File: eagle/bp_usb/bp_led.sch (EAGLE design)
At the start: 13 parts, among them J1 111-0703-001, J2 111-0702-001, J3 111-0703-001, J4 111-0702-001, J5 TSM-105-01-S-SV

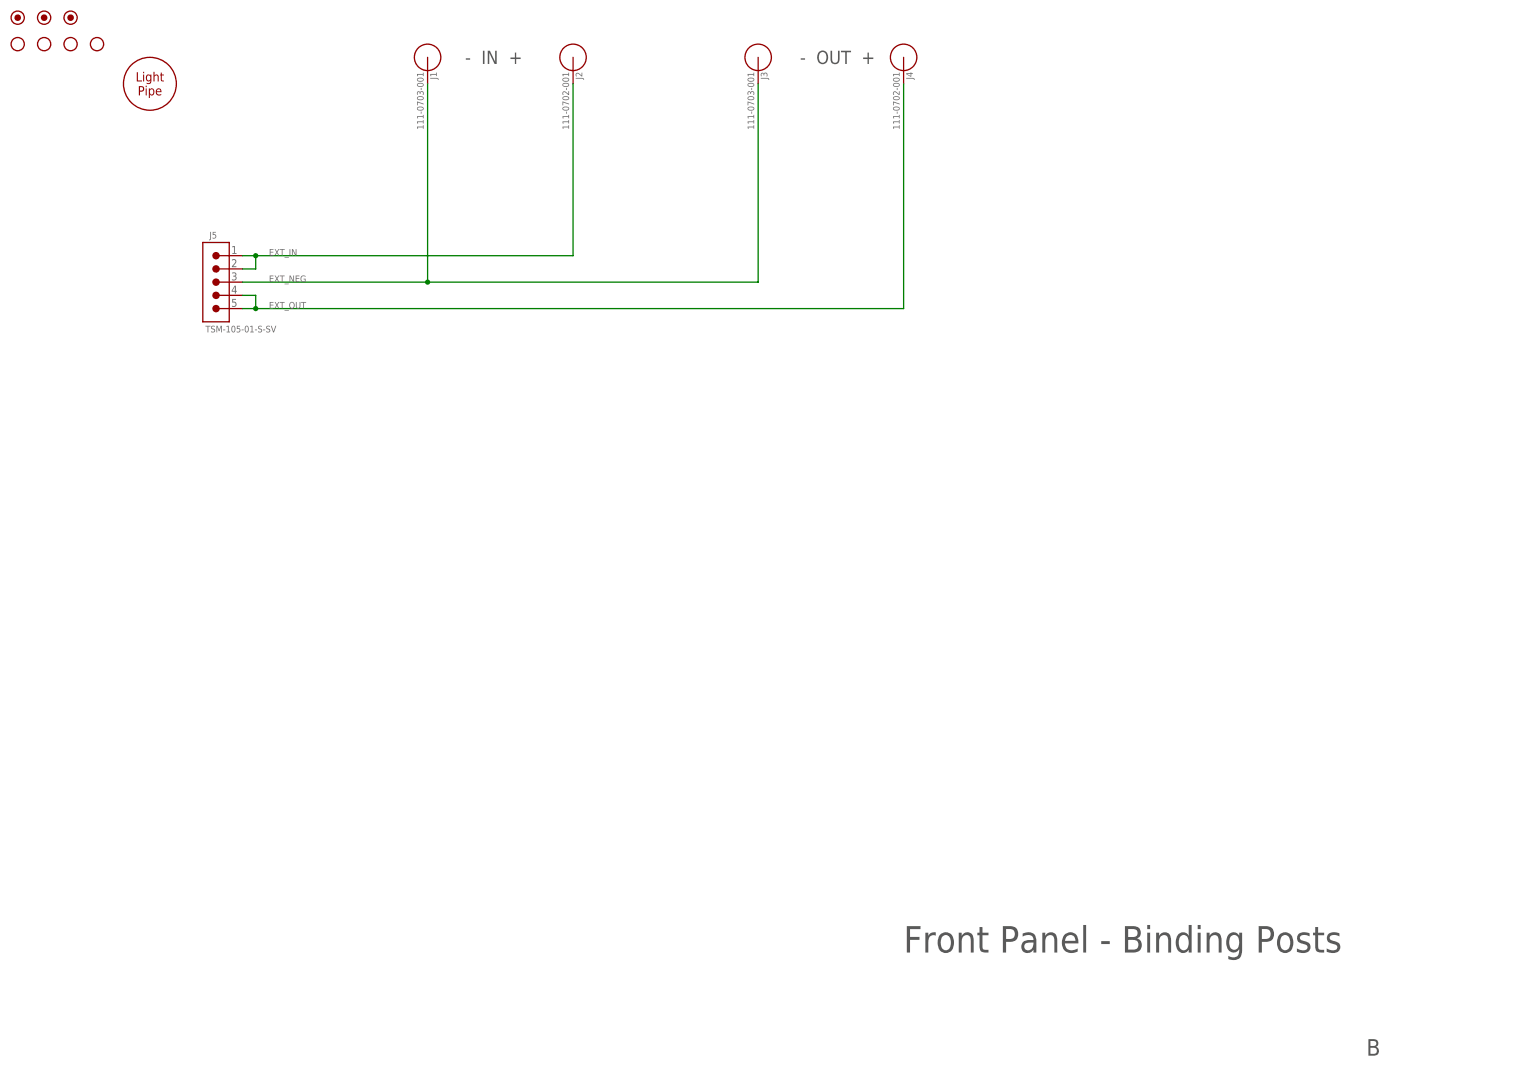
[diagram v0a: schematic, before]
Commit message: Pre-production update.
* Increased clearances from chassis/enclosure ground.
* Improved text.
* Added gerbers.
* Added USB back panel.
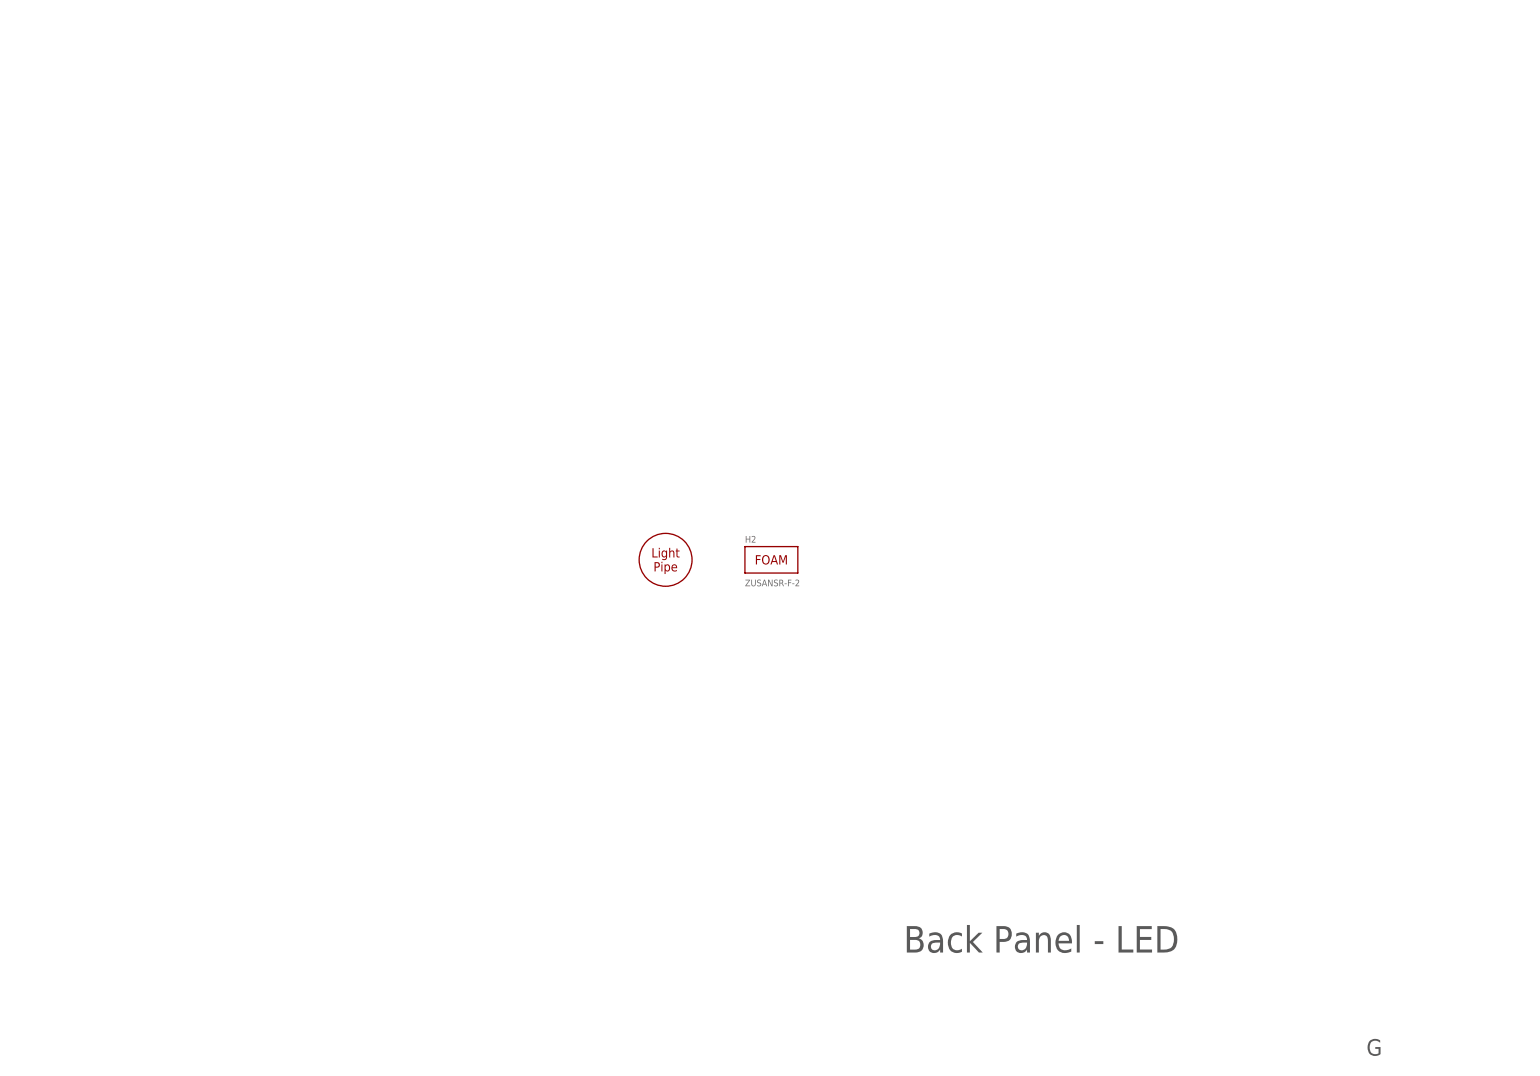
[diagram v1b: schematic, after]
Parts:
- removed FUD1, FUD2, FUD3: FIDUCIAL_1MM, jetperch:FIDUCIAL_1MM
- removed H3, H4, H5: HOLE_#6, jetperch:HOLE_#6
- removed J1, J3: 111-0703-001, jetperch:BINDING_POST_6
- removed J2, J4: 111-0702-001, jetperch:BINDING_POST_6
- removed J5: TSM-105-01-S-SV, jetperch:CONN_0.1_5X1_MS
- H2: value HOLE_#6 -> ZUSANSR-F-2; device jetperch:HOLE_#6 -> jetperch:FOAM_0.5_0.25; MPN (none) -> ZUSANSR-F-2; POPULATE (none) -> 1
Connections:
- removed net EXT_IN: J2.1, J5.1, J5.2
- removed net EXT_NEG: J1.1, J3.1, J5.3
- removed net EXT_OUT: J4.1, J5.4, J5.5
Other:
- note added: "Back Panel - LED"
- note added: "G"
- note removed: "- IN +"
- note removed: "- OUT +"
- note removed: "B"
- note removed: "Front Panel - Binding Posts"
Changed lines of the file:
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@@
 <class number="0" name="default" width="0" drill="0">
+</class>
+<class number="1" name="USBD" width="1.016" drill="0">
+<clearance class="0" value="0.1524"/>
+<clearance class="1" value="0.508"/>
 </class>
 </classes>
 <parts>
 <part name="FRAME1" library="frames" library_urn="urn:adsk.eagle:library:229" deviceset="FRAME_A_L" device="" value="PG1"/>
-<part name="J5" library="jetperch" deviceset="CONN_0.1_5X1" device="_MS" value="TSM-105-01-S-SV">
-<attribute name="MPN" value="TSM-105-01-S-SV"/>
-<attribute name="POPULATE" value="1"/>
-</part>
-<part name="J1" library="jetperch" deviceset="BINDING_POST" device="_6" value="111-0703-001">
-<attribute name="MPN" value=""/>
-<attribute name="POPULATE" value="1"/>
-</part>
-<part name="J2" library="jetperch" deviceset="BINDING_POST" device="_6" value="111-0702-001">
-<attribute name="MPN" value=""/>
-<attribute name="POPULATE" value="1"/>
-</part>
-<part name="J3" library="jetperch" deviceset="BINDING_POST" device="_6" value="111-0703-001">
-<attribute name="MPN" value=""/>
-<attribute name="POPULATE" value="1"/>
-</part>
-<part name="J4" library="jetperch" deviceset="BINDING_POST" device="_6" value="111-0702-001">
-<attribute name="MPN" value=""/>
-<attribute name="POPULATE" value="1"/>
-</part>
 <part name="H1" library="jetperch" deviceset="LIGHT_PIPE" device="_PANEL_3MM" value="51513020125F">
 <attribute name="MPN" value="51513020125F"/>
 </part>
-<part name="FUD1" library="jetperch" deviceset="FIDUCIAL" device="_1MM"/>
-<part name="FUD2" library="jetperch" deviceset="FIDUCIAL" device="_1MM"/>
-<part name="FUD3" library="jetperch" deviceset="FIDUCIAL" device="_1MM"/>
-<part name="H2" library="jetperch" deviceset="HOLE" device="_#6"/>
-<part name="H3" library="jetperch" deviceset="HOLE" device="_#6"/>
-<part name="H4" library="jetperch" deviceset="HOLE" device="_#6"/>
-<part name="H5" library="jetperch" deviceset="HOLE" device="_#6"/>
+<part name="H2" library="jetperch" deviceset="FOAM" device="_0.5_0.25" value="ZUSANSR-F-2">
+<attribute name="MPN" value="ZUSANSR-F-2"/>
+<attribute name="POPULATE" value="1"/>
+</part>
 </parts>
 <sheets>
 <sheet>
 <plain>
-<text x="177.8" y="26.162" size="5.08" layer="97">Front Panel - Binding Posts</text>
-<text x="266.7" y="6.35" size="3.175" layer="97">B</text>
-<text x="99.06" y="198.12" size="2.54" layer="97" align="center">-  IN  +</text>
-<text x="165.1" y="198.12" size="2.54" layer="97" align="center">-  OUT  +</text>
+<text x="177.8" y="26.162" size="5.08" layer="97">Back Panel - LED</text>
+<text x="266.7" y="6.35" size="3.175" layer="97">G</text>
 </plain>
 <instances>
@@
 <attribute name="DRAWING_NAME" x="190.5" y="19.05" size="2.54" layer="94"/>
 </instance>
-<instance part="J5" gate="G$1" x="45.72" y="154.94" smashed="yes">
-<attribute name="MPN" x="45.72" y="154.94" size="1.778" layer="96" display="off"/>
-<attribute name="POPULATE" x="45.72" y="154.94" size="1.778" layer="96" display="off"/>
-<attribute name="NAME" x="44.45" y="163.322" size="1.27" layer="95"/>
-<attribute name="VALUE" x="43.688" y="145.288" size="1.27" layer="96"/>
+<instance part="H1" gate="G$1" x="132.08" y="101.6" smashed="yes"/>
+<instance part="H2" gate="G$1" x="152.4" y="101.6" smashed="yes">
+<attribute name="NAME" x="147.32" y="104.902" size="1.27" layer="95"/>
+<attribute name="VALUE" x="147.32" y="96.52" size="1.27" layer="96"/>
+<attribute name="MPN" x="152.4" y="101.6" size="1.778" layer="96" display="off"/>
+<attribute name="POPULATE" x="152.4" y="101.6" size="1.778" layer="96" display="off"/>
 </instance>
-<instance part="J1" gate="G$1" x="86.36" y="198.12" smashed="yes" rot="R270">
-<attribute name="MPN" x="86.36" y="198.12" size="1.778" layer="96" display="off"/>
-<attribute name="POPULATE" x="86.36" y="198.12" size="1.778" layer="96" display="off"/>
-<attribute name="NAME" x="86.868" y="195.326" size="1.27" layer="95" rot="R270"/>
-<attribute name="VALUE" x="84.328" y="195.326" size="1.27" layer="96" rot="R270"/>
-</instance>
-<instance part="J2" gate="G$1" x="114.3" y="198.12" smashed="yes" rot="R270">
-<attribute name="MPN" x="114.3" y="198.12" size="1.778" layer="96" display="off"/>
-<attribute name="POPULATE" x="114.3" y="198.12" size="1.778" layer="96" display="off"/>
-<attribute name="NAME" x="114.808" y="195.326" size="1.27" layer="95" rot="R270"/>
-<attribute name="VALUE" x="112.268" y="195.326" size="1.27" layer="96" rot="R270"/>
-</instance>
-<instance part="J3" gate="G$1" x="149.86" y="198.12" smashed="yes" rot="R270">
-<attribute name="MPN" x="149.86" y="198.12" size="1.778" layer="96" display="off"/>
-<attribute name="POPULATE" x="149.86" y="198.12" size="1.778" layer="96" display="off"/>
-<attribute name="NAME" x="150.368" y="195.326" size="1.27" layer="95" rot="R270"/>
-<attribute name="VALUE" x="147.828" y="195.326" size="1.27" layer="96" rot="R270"/>
-</instance>
-<instance part="J4" gate="G$1" x="177.8" y="198.12" smashed="yes" rot="R270">
-<attribute name="MPN" x="177.8" y="198.12" size="1.778" layer="96" display="off"/>
-<attribute name="POPULATE" x="177.8" y="198.12" size="1.778" layer="96" display="off"/>
-<attribute name="NAME" x="178.308" y="195.326" size="1.27" layer="95" rot="R270"/>
-<attribute name="VALUE" x="175.768" y="195.326" size="1.27" layer="96" rot="R270"/>
-</instance>
-<instance part="H1" gate="G$1" x="33.02" y="193.04" smashed="yes"/>
-<instance part="FUD1" gate="G$1" x="7.62" y="205.74" smashed="yes"/>
-<instance part="FUD2" gate="G$1" x="12.7" y="205.74" smashed="yes"/>
-<instance part="FUD3" gate="G$1" x="17.78" y="205.74" smashed="yes"/>
-<instance part="H2" gate="G$1" x="7.62" y="200.66" smashed="yes"/>
-<instance part="H3" gate="G$1" x="12.7" y="200.66" smashed="yes"/>
-<instance part="H4" gate="G$1" x="17.78" y="200.66" smashed="yes"/>
-<instance part="H5" gate="G$1" x="22.86" y="200.66" smashed="yes"/>
 </instances>
 <busses>
 </busses>
 <nets>
-<net name="EXT_IN" class="0">
-<segment>
-<pinref part="J5" gate="G$1" pin="2"/>
-<wire x1="50.8" y1="157.48" x2="53.34" y2="157.48" width="0.1524" layer="91"/>
-<wire x1="53.34" y1="157.48" x2="53.34" y2="160.02" width="0.1524" layer="91"/>
-<pinref part="J5" gate="G$1" pin="1"/>
-<wire x1="53.34" y1="160.02" x2="50.8" y2="160.02" width="0.1524" layer="91"/>
-<label x="55.88" y="160.02" size="1.27" layer="95"/>
-<pinref part="J2" gate="G$1" pin="1"/>
-<wire x1="53.34" y1="160.02" x2="114.3" y2="160.02" width="0.1524" layer="91"/>
-<wire x1="114.3" y1="160.02" x2="114.3" y2="193.04" width="0.1524" layer="91"/>
-<junction x="53.34" y="160.02"/>
-</segment>
-</net>
-<net name="EXT_NEG" class="0">
-<segment>
-<pinref part="J5" gate="G$1" pin="3"/>
-<wire x1="50.8" y1="154.94" x2="86.36" y2="154.94" width="0.1524" layer="91"/>
-<label x="55.88" y="154.94" size="1.27" layer="95"/>
-<wire x1="86.36" y1="154.94" x2="86.36" y2="193.04" width="0.1524" layer="91"/>
-<pinref part="J1" gate="G$1" pin="1"/>
-<pinref part="J3" gate="G$1" pin="1"/>
-<wire x1="149.86" y1="193.04" x2="149.86" y2="154.94" width="0.1524" layer="91"/>
-<wire x1="149.86" y1="154.94" x2="86.36" y2="154.94" width="0.1524" layer="91"/>
-<junction x="86.36" y="154.94"/>
-</segment>
-</net>
-<net name="EXT_OUT" class="0">
-<segment>
-<pinref part="J5" gate="G$1" pin="5"/>
-<wire x1="50.8" y1="149.86" x2="53.34" y2="149.86" width="0.1524" layer="91"/>
-<wire x1="53.34" y1="149.86" x2="53.34" y2="152.4" width="0.1524" layer="91"/>
-<pinref part="J5" gate="G$1" pin="4"/>
-<wire x1="53.34" y1="152.4" x2="50.8" y2="152.4" width="0.1524" layer="91"/>
-<junction x="53.34" y="149.86"/>
-<label x="55.88" y="149.86" size="1.27" layer="95"/>
-<wire x1="53.34" y1="149.86" x2="177.8" y2="149.86" width="0.1524" layer="91"/>
-<pinref part="J4" gate="G$1" pin="1"/>
-<wire x1="177.8" y1="149.86" x2="177.8" y2="193.04" width="0.1524" layer="91"/>
-</segment>
-</net>
 </nets>
 </sheet>
